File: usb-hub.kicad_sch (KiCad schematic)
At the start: 37 parts, among them IC101 USB2517, J101 Barrel_Jack_Switch, J102 USB_C_Receptacle_USB2.0_14P, U101 USBLC6-2P6, Y101 24Mhz

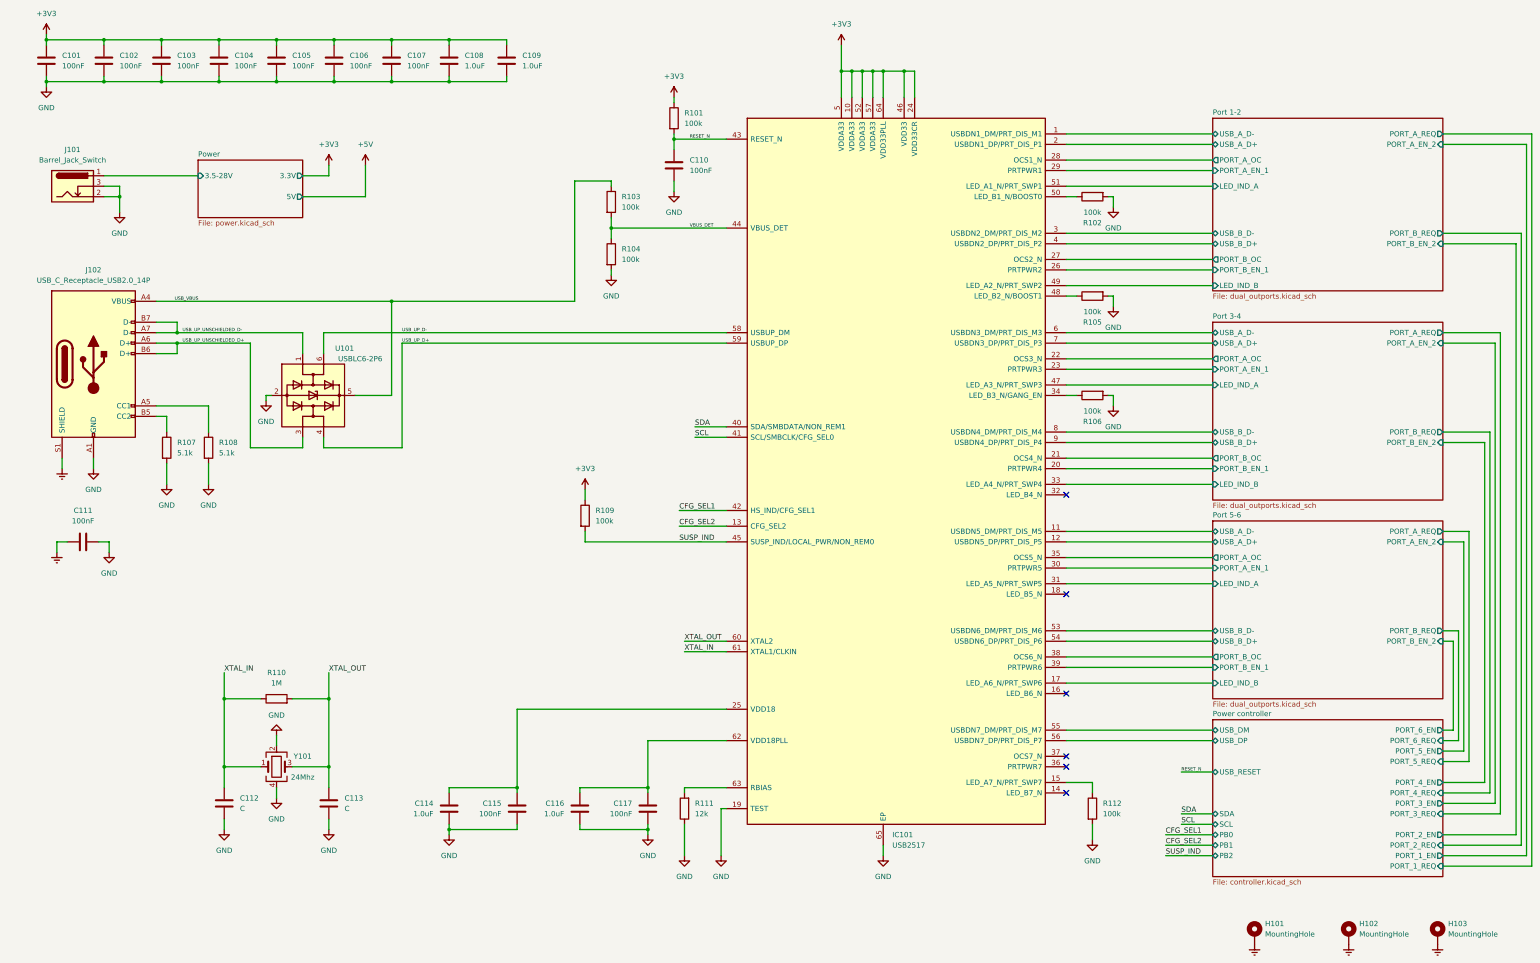
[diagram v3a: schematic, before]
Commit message: Finish first routing
Routed everything, so that the DRC and ERC do not show anything.
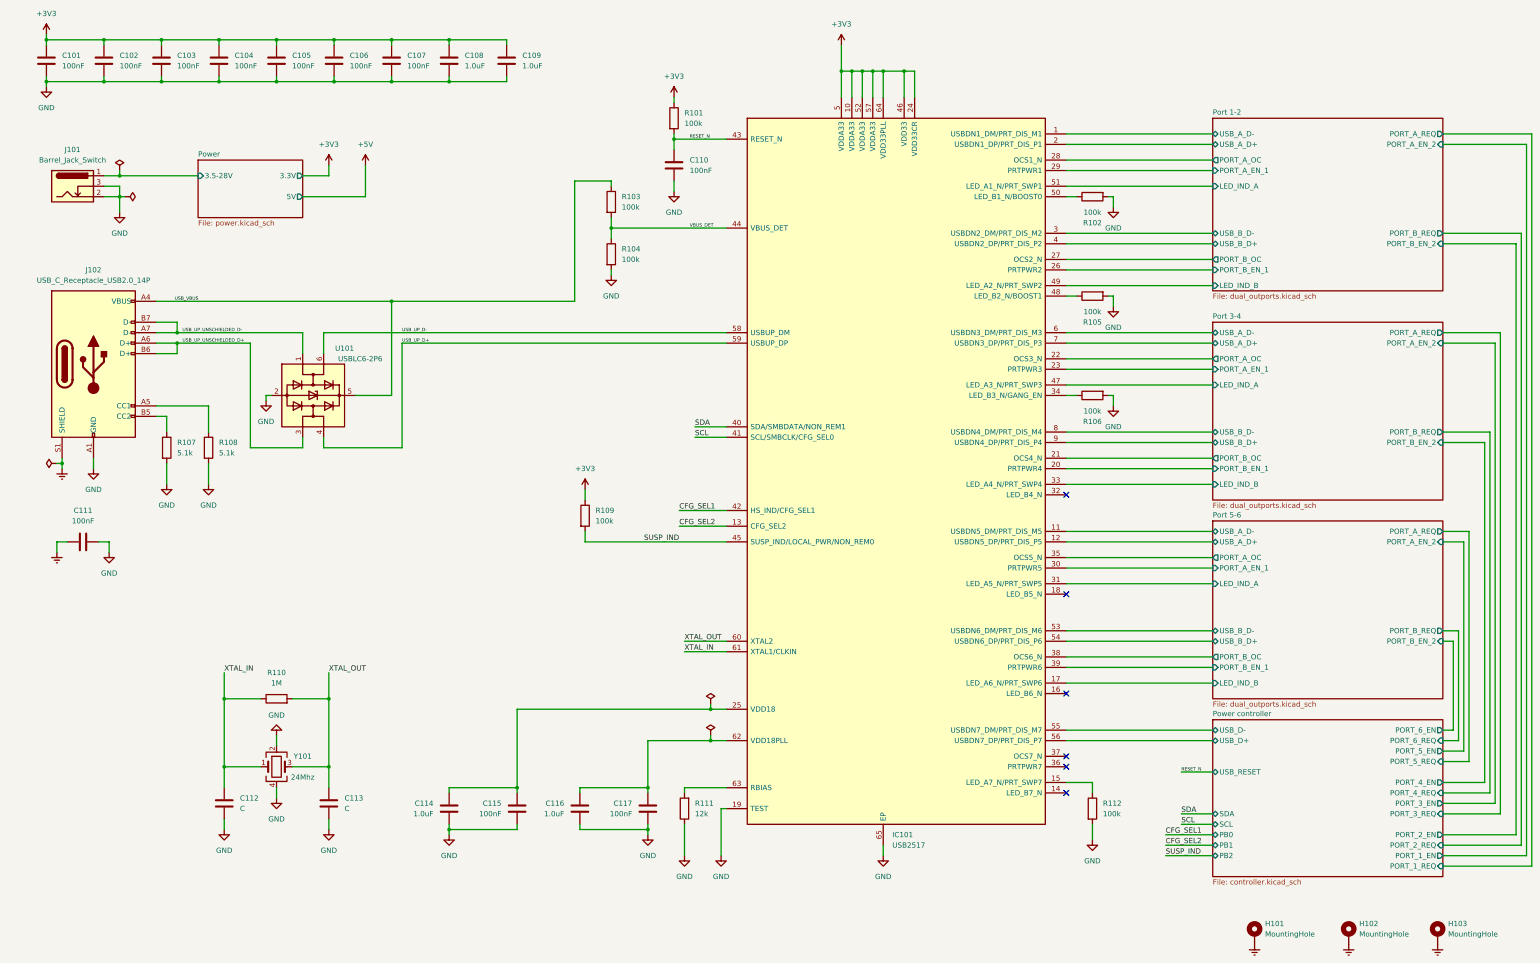
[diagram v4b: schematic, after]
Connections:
- net Power controller/USB_DM renamed Power controller/USB_D-
- net Power controller/USB_DP renamed Power controller/USB_D+
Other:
- sheet Power controller ports: added USB_D+, USB_D-; removed USB_DM, USB_DP
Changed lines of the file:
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@@
   (junction (at 67.31 186.69) (diameter 0) (color 0 0 0 0)
   )
+  (junction (at 185.42 196.85) (diameter 0) (color 0 0 0 0)
+  )
   (junction (at 121.92 36.83) (diameter 0) (color 0 0 0 0)
   )
@@
   (junction (at 107.95 36.83) (diameter 0) (color 0 0 0 0)
   )
+  (junction (at 41.91 59.69) (diameter 0) (color 0 0 0 0)
+  )
   (junction (at 67.31 203.2) (diameter 0) (color 0 0 0 0)
   )
@@
   (junction (at 55.88 97.79) (diameter 0) (color 0 0 0 0)
   )
+  (junction (at 27.94 129.54) (diameter 0) (color 0 0 0 0)
+  )
   (junction (at 92.71 203.2) (diameter 0) (color 0 0 0 0)
   )
@@
   (junction (at 93.98 26.67) (diameter 0) (color 0 0 0 0)
   )
+  (junction (at 185.42 189.23) (diameter 0) (color 0 0 0 0)
+  )
   (junction (at 224.79 34.29) (diameter 0) (color 0 0 0 0)
   )
@@
     (stroke (width 0) (type default))
   )
-  (wire (pts (xy 27.94 128.27) (xy 27.94 130.81))
+  (wire (pts (xy 27.94 128.27) (xy 27.94 129.54))
     (stroke (width 0) (type default))
   )
@@
     (stroke (width 0) (type default))
   )
-  (wire (pts (xy 138.43 189.23) (xy 189.23 189.23))
+  (wire (pts (xy 138.43 189.23) (xy 185.42 189.23))
     (stroke (width 0) (type default))
   )
@@
     (stroke (width 0) (type default))
   )
+  (wire (pts (xy 41.91 58.42) (xy 41.91 59.69))
+    (stroke (width 0) (type default))
+  )
   (wire (pts (xy 363.22 219.71) (xy 381 219.71))
     (stroke (width 0) (type default))
@@
     (stroke (width 0) (type default))
   )
+  (wire (pts (xy 185.42 187.96) (xy 185.42 189.23))
+    (stroke (width 0) (type default))
+  )
   (wire (pts (xy 91.44 102.87) (xy 91.44 97.79))
     (stroke (width 0) (type default))
@@
     (stroke (width 0) (type default))
   )
+  (wire (pts (xy 185.42 196.85) (xy 189.23 196.85))
+    (stroke (width 0) (type default))
+  )
   (wire (pts (xy 189.23 213.36) (xy 187.96 213.36))
     (stroke (width 0) (type default))
@@
     (stroke (width 0) (type default))
   )
+  (wire (pts (xy 27.94 129.54) (xy 27.94 130.81))
+    (stroke (width 0) (type default))
+  )
   (wire (pts (xy 363.22 227.33) (xy 384.81 227.33))
     (stroke (width 0) (type default))
@@
     (stroke (width 0) (type default))
   )
+  (wire (pts (xy 185.42 189.23) (xy 189.23 189.23))
+    (stroke (width 0) (type default))
+  )
   (wire (pts (xy 67.31 186.69) (xy 76.2 186.69))
     (stroke (width 0) (type default))
@@
     (stroke (width 0) (type default))
   )
+  (wire (pts (xy 43.18 64.77) (xy 41.91 64.77))
+    (stroke (width 0) (type default))
+  )
   (wire (pts (xy 73.66 100.33) (xy 73.66 125.73))
     (stroke (width 0) (type default))
@@
     (stroke (width 0) (type default))
   )
+  (wire (pts (xy 26.67 129.54) (xy 27.94 129.54))
+    (stroke (width 0) (type default))
+  )
   (wire (pts (xy 363.22 201.93) (xy 369.57 201.93))
     (stroke (width 0) (type default))
@@
     (stroke (width 0) (type default))
   )
-  (wire (pts (xy 38.1 59.69) (xy 60.96 59.69))
+  (wire (pts (xy 38.1 59.69) (xy 41.91 59.69))
     (stroke (width 0) (type default))
   )
-  (wire (pts (xy 170.18 196.85) (xy 189.23 196.85))
+  (wire (pts (xy 170.18 196.85) (xy 185.42 196.85))
     (stroke (width 0) (type default))
   )
@@
     (stroke (width 0) (type default))
   )
+  (wire (pts (xy 41.91 59.69) (xy 60.96 59.69))
+    (stroke (width 0) (type default))
+  )
   (wire (pts (xy 295.91 219.71) (xy 307.34 219.71))
     (stroke (width 0) (type default))
@@
     (stroke (width 0) (type default))
   )
+  (wire (pts (xy 185.42 195.58) (xy 185.42 196.85))
+    (stroke (width 0) (type default))
+  )
   (wire (pts (xy 55.88 95.25) (xy 55.88 97.79))
     (stroke (width 0) (type default))
@@
     (effects (font (size 1.27 1.27)) (justify left bottom))
   )
-  (label "SUSP_IND" (at 177.8 148.59 0) (fields_autoplaced)
-    (effects (font (size 1.27 1.27)) (justify left bottom))
+  (label "SUSP_IND" (at 177.8 148.59 180) (fields_autoplaced)
+    (effects (font (size 1.27 1.27)) (justify right bottom))
   )
   (label "XTAL_OUT" (at 179.07 172.72 0) (fields_autoplaced)
@@
     )
   )
+  (symbol (lib_id "power:PWR_FLAG") (at 185.42 195.58 0) (unit 1)
+    (in_bom yes) (on_board yes) (dnp no) (fields_autoplaced)
+    (property "Reference" "#FLG0102" (at 185.42 193.675 0)
+      (effects (font (size 1.27 1.27)) hide)
+    )
+    (property "Value" "PWR_FLAG" (at 185.42 190.5 0)
+      (effects (font (size 1.27 1.27)) hide)
+    )
+    (property "Footprint" "" (at 185.42 195.58 0)
+      (effects (font (size 1.27 1.27)) hide)
+    )
+    (property "Datasheet" "~" (at 185.42 195.58 0)
+      (effects (font (size 1.27 1.27)) hide)
+    )
+    (pin "1")
+    (instances
+      (project "usb-hub"
+        (path "/b46faf57-adcb-44f4-ac46-f905e4e8952b"
+          (reference "#FLG0102") (unit 1)
+        )
+      )
+    )
+  )
   (symbol (lib_id "Device:R") (at 278.13 64.77 90) (mirror x) (unit 1)
     (in_bom yes) (on_board yes) (dnp no)
@@
     )
   )
+  (symbol (lib_id "power:PWR_FLAG") (at 43.18 64.77 270) (unit 1)
+    (in_bom yes) (on_board yes) (dnp no) (fields_autoplaced)
+    (property "Reference" "#FLG0104" (at 45.085 64.77 0)
+      (effects (font (size 1.27 1.27)) hide)
+    )
+    (property "Value" "PWR_FLAG" (at 48.26 64.77 0)
+      (effects (font (size 1.27 1.27)) hide)
+    )
+    (property "Footprint" "" (at 43.18 64.77 0)
+      (effects (font (size 1.27 1.27)) hide)
+    )
+    (property "Datasheet" "~" (at 43.18 64.77 0)
+      (effects (font (size 1.27 1.27)) hide)
+    )
+    (pin "1")
+    (instances
+      (project "usb-hub"
+        (path "/b46faf57-adcb-44f4-ac46-f905e4e8952b"
+          (reference "#FLG0104") (unit 1)
+        )
+      )
+    )
+  )
   (symbol (lib_id "power:GND") (at 67.31 218.44 0) (unit 1)
     (in_bom yes) (on_board yes) (dnp no) (fields_autoplaced)
@@
     )
   )
+  (symbol (lib_id "power:PWR_FLAG") (at 26.67 129.54 90) (unit 1)
+    (in_bom yes) (on_board yes) (dnp no) (fields_autoplaced)
+    (property "Reference" "#FLG0105" (at 24.765 129.54 0)
+      (effects (font (size 1.27 1.27)) hide)
+    )
+    (property "Value" "PWR_FLAG" (at 21.59 129.54 0)
+      (effects (font (size 1.27 1.27)) hide)
+    )
+    (property "Footprint" "" (at 26.67 129.54 0)
+      (effects (font (size 1.27 1.27)) hide)
+    )
+    (property "Datasheet" "~" (at 26.67 129.54 0)
+      (effects (font (size 1.27 1.27)) hide)
+    )
+    (pin "1")
+    (instances
+      (project "usb-hub"
+        (path "/b46faf57-adcb-44f4-ac46-f905e4e8952b"
+          (reference "#FLG0105") (unit 1)
+        )
+      )
+    )
+  )
   (symbol (lib_id "Device:R") (at 161.29 78.74 0) (unit 1)
     (in_bom yes) (on_board yes) (dnp no) (fields_autoplaced)
@@
     )
   )
+  (symbol (lib_id "power:PWR_FLAG") (at 41.91 58.42 0) (unit 1)
+    (in_bom yes) (on_board yes) (dnp no) (fields_autoplaced)
+    (property "Reference" "#FLG0103" (at 41.91 56.515 0)
+      (effects (font (size 1.27 1.27)) hide)
+    )
+    (property "Value" "PWR_FLAG" (at 41.91 53.34 0)
+      (effects (font (size 1.27 1.27)) hide)
+    )
+    (property "Footprint" "" (at 41.91 58.42 0)
+      (effects (font (size 1.27 1.27)) hide)
+    )
+    (property "Datasheet" "~" (at 41.91 58.42 0)
+      (effects (font (size 1.27 1.27)) hide)
+    )
+    (pin "1")
+    (instances
+      (project "usb-hub"
+        (path "/b46faf57-adcb-44f4-ac46-f905e4e8952b"
+          (reference "#FLG0103") (unit 1)
+        )
+      )
+    )
+  )
   (symbol (lib_id "Mechanical:MountingHole_Pad") (at 361.95 243.84 0) (unit 1)
     (in_bom no) (on_board yes) (dnp no) (fields_autoplaced)
@@
     )
   )
+  (symbol (lib_id "power:PWR_FLAG") (at 185.42 187.96 0) (unit 1)
+    (in_bom yes) (on_board yes) (dnp no) (fields_autoplaced)
+    (property "Reference" "#FLG0101" (at 185.42 186.055 0)
+      (effects (font (size 1.27 1.27)) hide)
+    )
+    (property "Value" "PWR_FLAG" (at 185.42 182.88 0)
+      (effects (font (size 1.27 1.27)) hide)
+    )
+    (property "Footprint" "" (at 185.42 187.96 0)
+      (effects (font (size 1.27 1.27)) hide)
+    )
+    (property "Datasheet" "~" (at 185.42 187.96 0)
+      (effects (font (size 1.27 1.27)) hide)
+    )
+    (pin "1")
+    (instances
+      (project "usb-hub"
+        (path "/b46faf57-adcb-44f4-ac46-f905e4e8952b"
+          (reference "#FLG0101") (unit 1)
+        )
+      )
+    )
+  )
   (symbol (lib_id "power:GND") (at 283.21 91.44 0) (unit 1)
     (in_bom yes) (on_board yes) (dnp no) (fields_autoplaced)
@@
       (effects (font (size 1.27 1.27)) (justify left top))
     )
-    (pin "USB_DM" bidirectional (at 307.34 194.31 180)
-      (effects (font (size 1.27 1.27)) (justify left))
-    )
-    (pin "USB_DP" bidirectional (at 307.34 196.85 180)
-      (effects (font (size 1.27 1.27)) (justify left))
-    )
     (pin "PORT_2_EN" output (at 363.22 219.71 0)
       (effects (font (size 1.27 1.27)) (justify right))
@@
       (effects (font (size 1.27 1.27)) (justify left))
     )
+    (pin "USB_D-" bidirectional (at 307.34 194.31 180)
+      (effects (font (size 1.27 1.27)) (justify left))
+    )
+    (pin "USB_D+" bidirectional (at 307.34 196.85 180)
+      (effects (font (size 1.27 1.27)) (justify left))
+    )

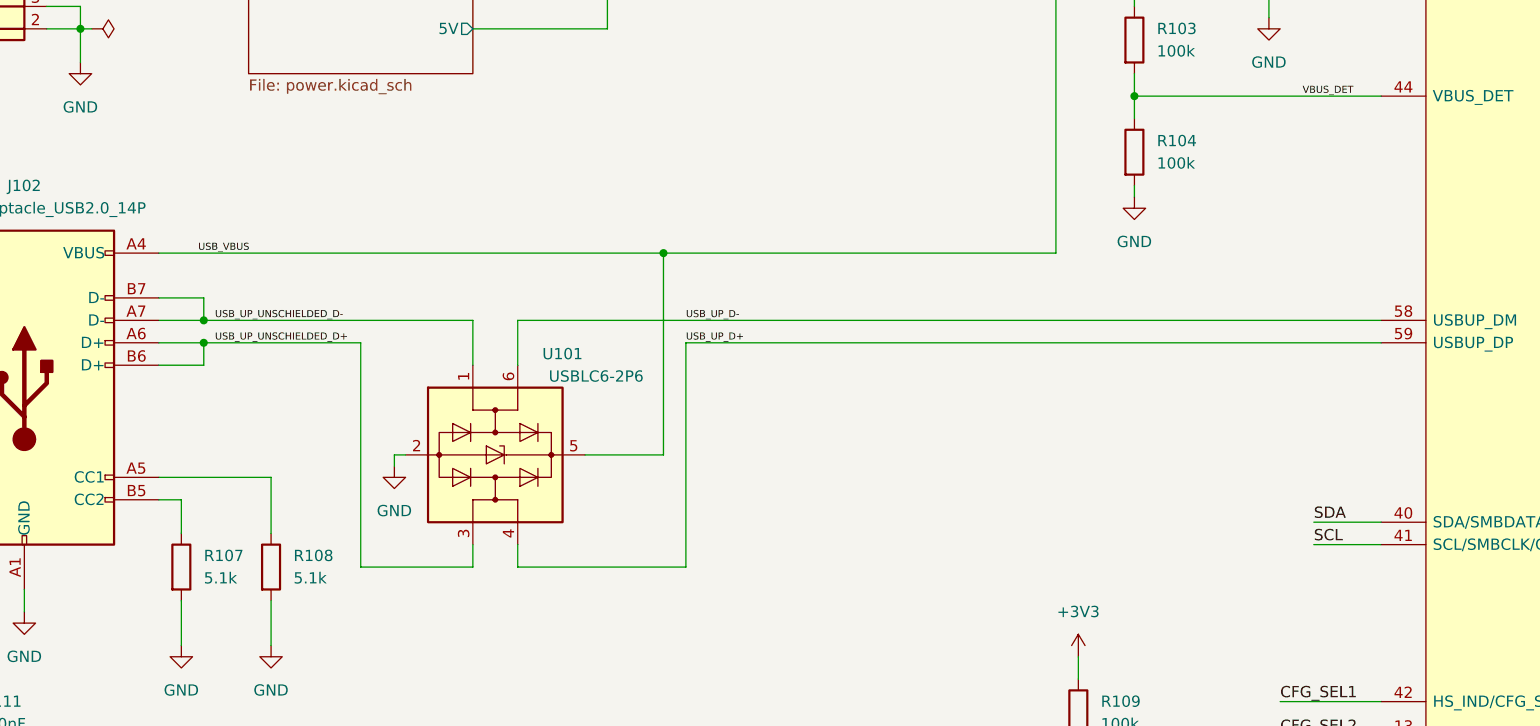
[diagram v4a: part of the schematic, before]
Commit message: Update to new enviroment
Kicad 8 & global symbols and footprint library
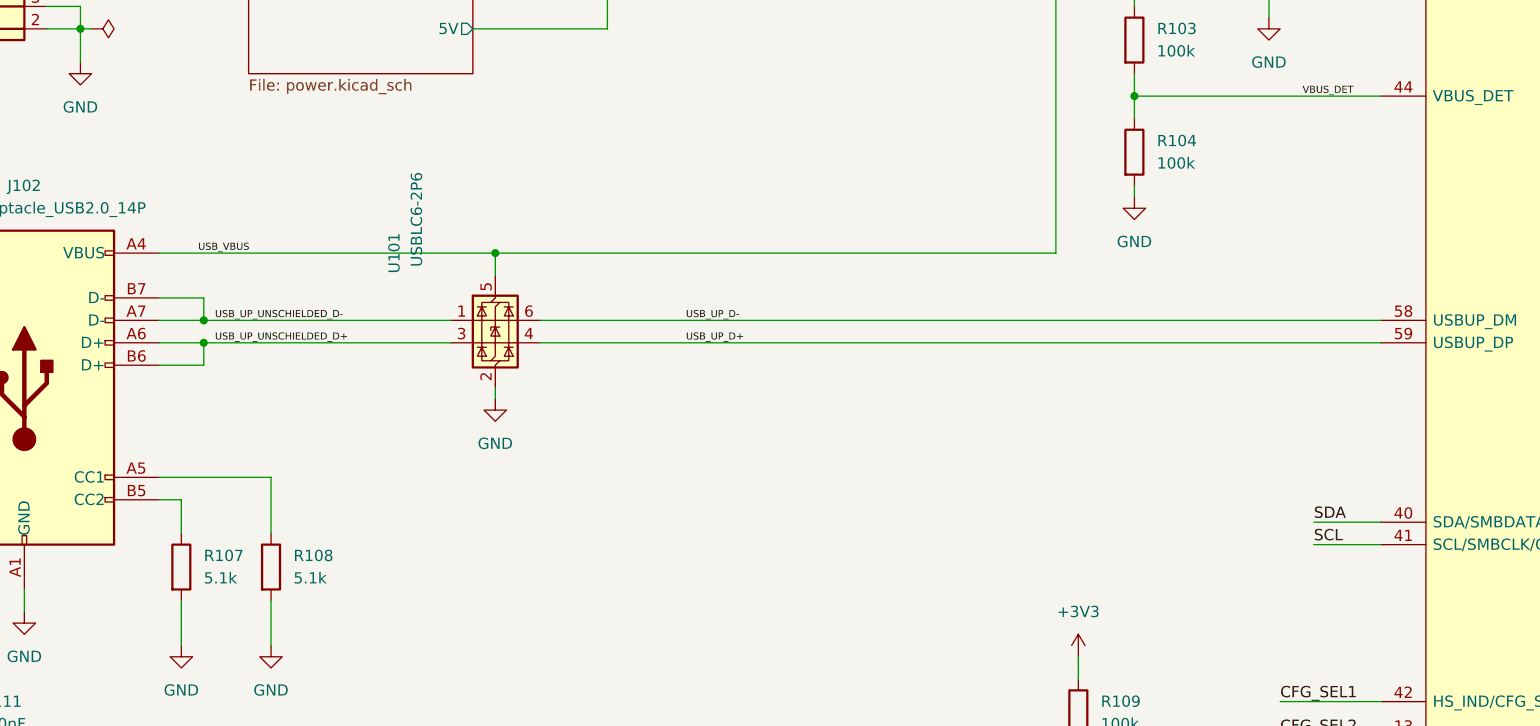
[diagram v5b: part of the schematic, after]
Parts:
- IC101: symbol fabian_usb:USB2517 -> g-usb:USB2517
